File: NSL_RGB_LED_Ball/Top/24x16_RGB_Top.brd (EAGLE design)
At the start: 48 x 48 mm, 20 parts

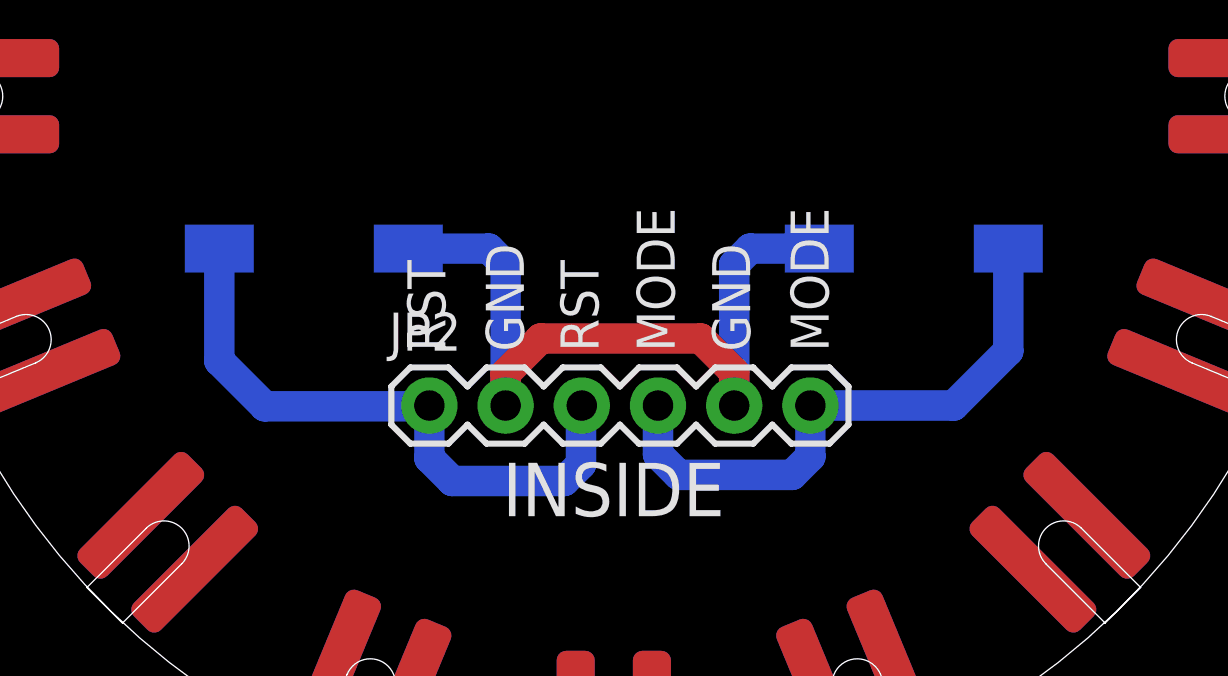
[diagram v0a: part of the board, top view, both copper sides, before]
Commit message: 
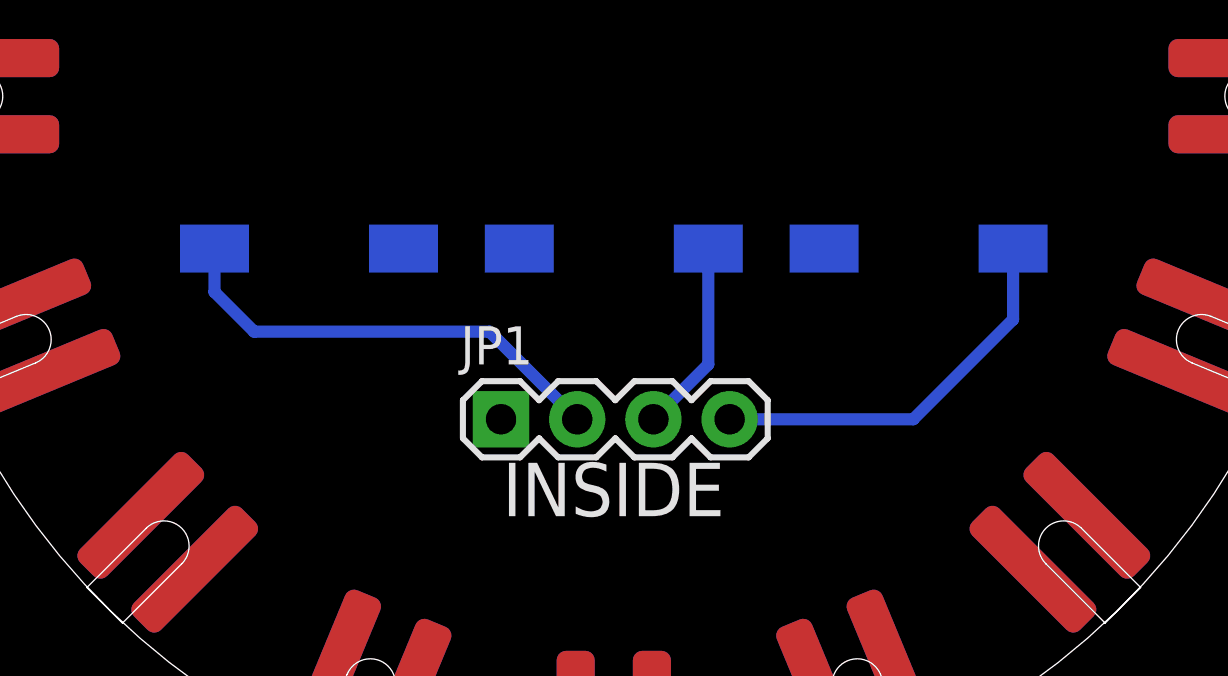
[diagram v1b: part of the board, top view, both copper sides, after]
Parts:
- removed JP2: (no value), SparkFun-Connectors:1X06
- added JP1: (no value), SparkFun-Connectors:1X04
- added S3: SPARKFUN-ELECTROMECHANICAL_SWITCH-MOMENTARY-2-SMD-1101NE, tvbgone-2layer:SPARKFUN-ELECTROMECHANICAL_TACTILE-SWITCH-1101NE
- moved S1 10.0 mm to (0.00, -5.08)
- moved S2 0.16 mm to (-10.2, -5.08)
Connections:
- removed net MODE: JP2.4, JP2.6, S1.P$1
- removed net RST: JP2.1, JP2.3, S2.P$1
- new net DOWN: JP1.2, S2.P$1
- new net SELECT: JP1.3, S1.P$1
- new net UP: JP1.4, S3.P$1
- net GND: now also JP1.1, S3.P$2; no longer JP2.2, JP2.5
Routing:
- net GND: track 26.7 -> 0.00 mm
- net RST: track 20.7 -> 0.00 mm
- net MODE: track 19.7 -> 0.00 mm
- net DOWN: track 0.00 -> 15.3 mm
- net UP: track 0.00 -> 13.2 mm
- net SELECT: track 0.00 -> 6.45 mm
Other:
- board text added: "DOWN"
- board text added: "SELECT"
- board text added: "UP"
- board text removed: "GND"
- board text removed: "MODE"
- board text removed: "Mode"
- board text removed: "RST"
- board text removed: "Reset"
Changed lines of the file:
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@@
 <wire x1="24" y1="0" x2="24" y2="0.01" width="0" layer="20" curve="-359.976127"/>
 <dimension x1="0" y1="-24" x2="0" y2="-21.16" x3="12.97" y3="-22.58" textsize="1.778" layer="48"/>
-<text x="-7.0612" y="-8.89" size="1.778" layer="22" font="vector" rot="MR0">Reset</text>
-<text x="13.081" y="-8.89" size="1.778" layer="22" font="vector" rot="MR0">Mode</text>
-<text x="-5.6134" y="-8.509" size="1.27" layer="21" font="vector" rot="R90">RST</text>
-<text x="-2.9972" y="-8.509" size="1.27" layer="21" font="vector" rot="R90">GND</text>
-<text x="2.032" y="-8.509" size="1.27" layer="21" font="vector" rot="R90">MODE</text>
-<text x="4.5466" y="-8.509" size="1.27" layer="21" font="vector" rot="R90">GND</text>
-<text x="7.1628" y="-8.509" size="1.27" layer="21" font="vector" rot="R90">MODE</text>
-<text x="-0.508" y="-8.509" size="1.27" layer="21" font="vector" rot="R90">RST</text>
 <text x="0" y="0" size="2.032" layer="22" font="vector" rot="MR0" align="center">nullspacelabs.com</text>
+<text x="11.3792" y="-9.144" size="1.778" layer="22" font="vector" rot="MR0">UP</text>
+<text x="4.6736" y="-9.144" size="1.778" layer="22" font="vector" rot="MR0">SELECT</text>
+<text x="-7.1628" y="-9.144" size="1.778" layer="22" font="vector" rot="MR0">DOWN</text>
 </plain>
 <attributes>
@@
 <attribute name="MF" value="" x="56.63675625" y="-45.45391875" size="1.778" layer="27" rot="R157.5" display="off"/>
 </element>
-<element name="S1" library="tvbgone-2layer" package="SPARKFUN-ELECTROMECHANICAL_TACTILE-SWITCH-1101NE" value="SPARKFUN-ELECTROMECHANICAL_SWITCH-MOMENTARY-2-SMD-1101NE" x="10" y="-5.08" rot="MR0"/>
-<element name="S2" library="tvbgone-2layer" package="SPARKFUN-ELECTROMECHANICAL_TACTILE-SWITCH-1101NE" value="SPARKFUN-ELECTROMECHANICAL_SWITCH-MOMENTARY-2-SMD-1101NE" x="-10" y="-5.08" rot="MR180"/>
-<element name="JP2" library="SparkFun-Connectors" package="1X06" value="" x="-6.1468" y="-10.3124"/>
+<element name="S1" library="tvbgone-2layer" package="SPARKFUN-ELECTROMECHANICAL_TACTILE-SWITCH-1101NE" value="SPARKFUN-ELECTROMECHANICAL_SWITCH-MOMENTARY-2-SMD-1101NE" x="0" y="-5.08" rot="MR0"/>
+<element name="S2" library="tvbgone-2layer" package="SPARKFUN-ELECTROMECHANICAL_TACTILE-SWITCH-1101NE" value="SPARKFUN-ELECTROMECHANICAL_SWITCH-MOMENTARY-2-SMD-1101NE" x="-10.16" y="-5.08" rot="MR180"/>
 <element name="U$1" library="24x16_RGB_Bottom" package="USB_PANNEL" value="USB_PANNEL" x="0" y="9.525"/>
+<element name="JP1" library="SparkFun-Connectors" package="1X04" value="" x="-3.7592" y="-10.7696"/>
+<element name="S3" library="tvbgone-2layer" package="SPARKFUN-ELECTROMECHANICAL_TACTILE-SWITCH-1101NE" value="SPARKFUN-ELECTROMECHANICAL_SWITCH-MOMENTARY-2-SMD-1101NE" x="10.16" y="-5.08" rot="MR0"/>
 </elements>
 <signals>
 <signal name="SLOT">
 </signal>
-<signal name="MODE">
-<contactref element="S1" pad="P$1"/>
-<contactref element="JP2" pad="6"/>
-<contactref element="JP2" pad="4"/>
-<wire x1="13.15" y1="-5.08" x2="13.15" y2="-8.4908" width="1.016" layer="16"/>
-<wire x1="13.15" y1="-8.4908" x2="11.3284" y2="-10.3124" width="1.016" layer="16"/>
-<wire x1="11.3284" y1="-10.3124" x2="6.5532" y2="-10.3124" width="1.016" layer="16"/>
-<wire x1="6.5532" y1="-10.3124" x2="6.5532" y2="-12.0142" width="1.016" layer="16"/>
-<wire x1="6.5532" y1="-12.0142" x2="5.9436" y2="-12.6238" width="1.016" layer="16"/>
-<wire x1="5.9436" y1="-12.6238" x2="2.159" y2="-12.6238" width="1.016" layer="16"/>
-<wire x1="2.159" y1="-12.6238" x2="1.4732" y2="-11.938" width="1.016" layer="16"/>
-<wire x1="1.4732" y1="-11.938" x2="1.4732" y2="-10.3124" width="1.016" layer="16"/>
-</signal>
-<signal name="RST">
-<contactref element="S2" pad="P$1"/>
-<contactref element="JP2" pad="1"/>
-<contactref element="JP2" pad="3"/>
-<wire x1="-13.15" y1="-5.08" x2="-13.15" y2="-8.821" width="1.016" layer="16"/>
-<wire x1="-13.15" y1="-8.821" x2="-11.6332" y2="-10.3378" width="1.016" layer="16"/>
-<wire x1="-11.6332" y1="-10.3378" x2="-6.1722" y2="-10.3378" width="1.016" layer="16"/>
-<wire x1="-6.1722" y1="-10.3378" x2="-6.1468" y2="-10.3124" width="1.016" layer="16"/>
-<wire x1="-6.1468" y1="-10.3124" x2="-6.1468" y2="-12.065" width="1.016" layer="16"/>
-<wire x1="-6.1468" y1="-12.065" x2="-5.3848" y2="-12.827" width="1.016" layer="16"/>
-<wire x1="-5.3848" y1="-12.827" x2="-1.651" y2="-12.827" width="1.016" layer="16"/>
-<wire x1="-1.651" y1="-12.827" x2="-1.0922" y2="-12.2682" width="1.016" layer="16"/>
-<wire x1="-1.0922" y1="-12.2682" x2="-1.0922" y2="-10.3378" width="1.016" layer="16"/>
-<wire x1="-1.0922" y1="-10.3378" x2="-1.0668" y2="-10.3124" width="1.016" layer="16"/>
-</signal>
 <signal name="GND">
 <contactref element="S1" pad="P$2"/>
 <contactref element="S2" pad="P$2"/>
-<contactref element="JP2" pad="5"/>
-<contactref element="JP2" pad="2"/>
-<wire x1="6.85" y1="-5.08" x2="4.5466" y2="-5.08" width="1.016" layer="16"/>
-<wire x1="4.5466" y1="-5.08" x2="4.0132" y2="-5.6134" width="1.016" layer="16"/>
-<wire x1="4.0132" y1="-5.6134" x2="4.0132" y2="-10.3124" width="1.016" layer="16"/>
-<wire x1="-6.85" y1="-5.08" x2="-4.1656" y2="-5.08" width="1.016" layer="16"/>
-<wire x1="-4.1656" y1="-5.08" x2="-3.6068" y2="-5.6388" width="1.016" layer="16"/>
-<wire x1="-3.6068" y1="-5.6388" x2="-3.6068" y2="-10.3124" width="1.016" layer="16"/>
-<wire x1="-3.6068" y1="-10.3124" x2="-3.6068" y2="-9.2456" width="1.016" layer="1"/>
-<wire x1="-3.6068" y1="-9.2456" x2="-2.4384" y2="-8.0772" width="1.016" layer="1"/>
-<wire x1="-2.4384" y1="-8.0772" x2="2.8956" y2="-8.0772" width="1.016" layer="1"/>
-<wire x1="2.8956" y1="-8.0772" x2="4.0132" y2="-9.1948" width="1.016" layer="1"/>
-<wire x1="4.0132" y1="-9.1948" x2="4.0132" y2="-10.3124" width="1.016" layer="1"/>
 <contactref element="SLOT1" pad="P$3"/>
 <contactref element="SLOT1" pad="P$4"/>
@@
 <vertex x="25.811" y="27.0204"/>
 </polygon>
+<contactref element="JP1" pad="1"/>
+<contactref element="S3" pad="P$2"/>
 </signal>
 <signal name="BLANK">
@@
 </polygon>
 </signal>
+<signal name="UP">
+<contactref element="JP1" pad="4"/>
+<contactref element="S3" pad="P$1"/>
+<wire x1="3.8608" y1="-10.7696" x2="9.9822" y2="-10.7696" width="0.4064" layer="16"/>
+<wire x1="9.9822" y1="-10.7696" x2="13.3096" y2="-7.4422" width="0.4064" layer="16"/>
+<wire x1="13.3096" y1="-7.4422" x2="13.3096" y2="-5.0804" width="0.4064" layer="16"/>
+<wire x1="13.3096" y1="-5.0804" x2="13.31" y2="-5.08" width="0.4064" layer="16"/>
+</signal>
+<signal name="SELECT">
+<contactref element="JP1" pad="3"/>
+<contactref element="S1" pad="P$1"/>
+<wire x1="1.3208" y1="-10.7696" x2="3.15" y2="-8.9404" width="0.4064" layer="16"/>
+<wire x1="3.15" y1="-8.9404" x2="3.15" y2="-5.08" width="0.4064" layer="16"/>
+</signal>
+<signal name="DOWN">
+<contactref element="JP1" pad="2"/>
+<contactref element="S2" pad="P$1"/>
+<wire x1="-1.2192" y1="-10.7696" x2="-4.1402" y2="-7.8486" width="0.4064" layer="16"/>
+<wire x1="-4.1402" y1="-7.8486" x2="-11.9888" y2="-7.8486" width="0.4064" layer="16"/>
+<wire x1="-11.9888" y1="-7.8486" x2="-13.31" y2="-6.5274" width="0.4064" layer="16"/>
+<wire x1="-13.31" y1="-6.5274" x2="-13.31" y2="-5.08" width="0.4064" layer="16"/>
+</signal>
 </signals>

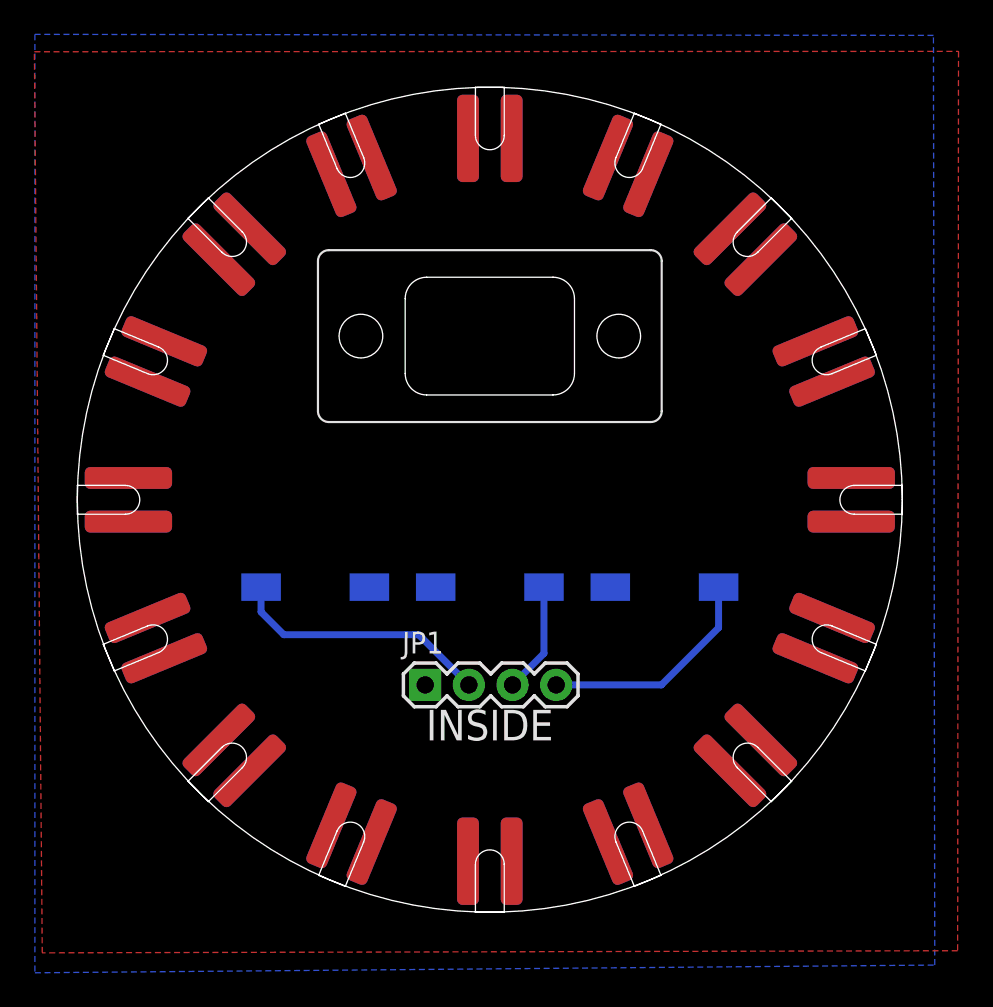
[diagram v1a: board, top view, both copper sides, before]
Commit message: 
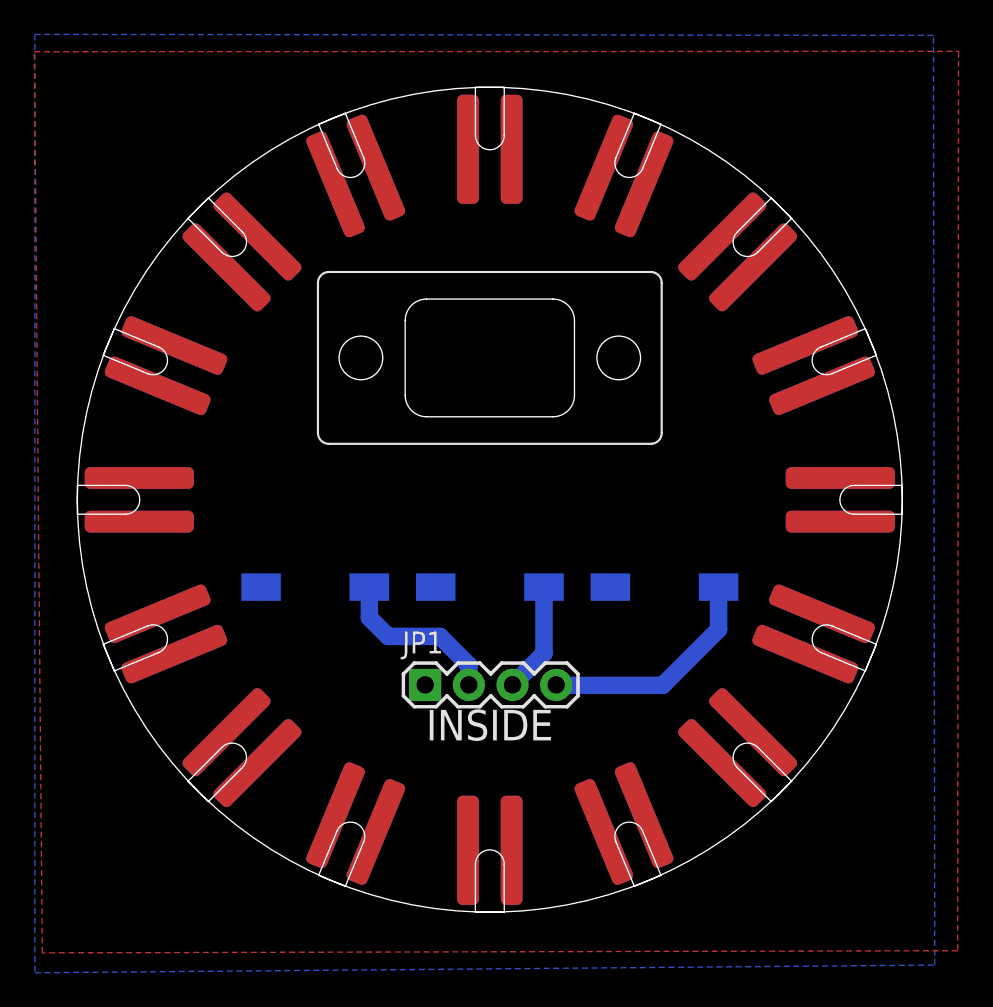
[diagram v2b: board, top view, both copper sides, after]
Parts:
- SLOT1, SLOT10, SLOT11, SLOT12, SLOT13, SLOT14, SLOT15, SLOT16, SLOT2, SLOT3, SLOT4, SLOT5, SLOT6, SLOT7, SLOT8, SLOT9: device 24x16_RGB_Bottom:SLOT -> 24x16_RGB_Top:SLOT
- moved U$1 1.27 mm to (0.00, 8.26)
- turned S2 to 0 degrees
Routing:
- net DOWN: track 15.3 -> 9.86 mm

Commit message: 
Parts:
- removed JP1: (no value), SparkFun-Connectors:1X04
- added JP2: (no value), SparkFun-Connectors:1X06
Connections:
- net DOWN: now also JP2.4; no longer JP1.2
- net GND: now also JP2.1, JP2.2, JP2.3; no longer JP1.1
- net SELECT: now also JP2.5; no longer JP1.3
- net UP: now also JP2.6; no longer JP1.4
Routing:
- net UP: track 13.3 -> 9.32 mm
- net DOWN: track 9.86 -> 10.8 mm
- net SELECT: track 6.45 -> 5.90 mm
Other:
- board text added: "DWN"
- board text added: "GND"
- board text added: "SEL"
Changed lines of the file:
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@@
 <plain>
 <text x="0" y="-15.2108" size="1.778" layer="22" rot="MR0" align="center">A</text>
-<text x="-3.71" y="-14" size="1.778" layer="21">INSIDE</text>
+<text x="-3.6592" y="-3.1796" size="1.778" layer="21">INSIDE</text>
 <wire x1="24" y1="0" x2="24" y2="0.01" width="0" layer="20" curve="-359.976127"/>
 <dimension x1="0" y1="-24" x2="0" y2="-21.16" x3="12.97" y3="-22.58" textsize="1.778" layer="48"/>
@@
 <text x="4.6736" y="-9.144" size="1.778" layer="22" font="vector" rot="MR0">SELECT</text>
 <text x="-7.1628" y="-9.144" size="1.778" layer="22" font="vector" rot="MR0">DOWN</text>
+<text x="0.381" y="-12.065" size="1.778" layer="21" font="vector" rot="R270">DWN</text>
+<text x="2.9718" y="-12.065" size="1.778" layer="21" font="vector" rot="R270">SEL</text>
+<text x="5.6388" y="-12.065" size="1.778" layer="21" font="vector" rot="R270">UP</text>
+<text x="-2.1336" y="-12.065" size="1.778" layer="21" font="vector" rot="R270">GND</text>
+<text x="-4.6482" y="-12.065" size="1.778" layer="21" font="vector" rot="R270">GND</text>
+<text x="-7.2644" y="-12.065" size="1.778" layer="21" font="vector" rot="R270">GND</text>
 </plain>
 <attributes>
@@
 </element>
 <element name="U$1" library="24x16_RGB_Bottom" package="USB_PANNEL" value="USB_PANNEL" x="0" y="8.255"/>
-<element name="JP1" library="SparkFun-Connectors" package="1X04" value="" x="-3.7592" y="-10.7696"/>
 <element name="S3" library="tvbgone-2layer" package="SPARKFUN-ELECTROMECHANICAL_TACTILE-SWITCH-1101NE" value="SPARKFUN-ELECTROMECHANICAL_SWITCH-MOMENTARY-2-SMD-1101NE" x="10.16" y="-5.08" smashed="yes" rot="MR0">
 <attribute name="NAME" x="13.16" y="-3.08" size="0.762" layer="26" rot="MR0"/>
 </element>
+<element name="JP2" library="SparkFun-Connectors" package="1X06" value="" x="-6.3754" y="-10.7188"/>
 </elements>
 <signals>
@@
 <vertex x="25.811" y="27.0204"/>
 </polygon>
-<contactref element="JP1" pad="1"/>
 <contactref element="S3" pad="P$2"/>
+<contactref element="JP2" pad="3"/>
+<contactref element="JP2" pad="2"/>
+<contactref element="JP2" pad="1"/>
 </signal>
 <signal name="BLANK">
@@
 </signal>
 <signal name="UP">
-<contactref element="JP1" pad="4"/>
 <contactref element="S3" pad="P$1"/>
 <wire x1="13.3096" y1="-5.0804" x2="13.31" y2="-5.08" width="0.4064" layer="16"/>
-<wire x1="3.8608" y1="-10.7696" x2="3.8862" y2="-10.795" width="1.016" layer="16"/>
-<wire x1="3.8862" y1="-10.795" x2="10.0584" y2="-10.795" width="1.016" layer="16"/>
-<wire x1="10.0584" y1="-10.795" x2="13.31" y2="-7.5434" width="1.016" layer="16"/>
-<wire x1="13.31" y1="-7.5434" x2="13.31" y2="-5.08" width="1.016" layer="16"/>
+<contactref element="JP2" pad="6"/>
+<wire x1="13.31" y1="-5.08" x2="7.6712" y2="-10.7188" width="0.4064" layer="16"/>
+<wire x1="7.6712" y1="-10.7188" x2="6.3246" y2="-10.7188" width="0.4064" layer="16"/>
 </signal>
 <signal name="SELECT">
-<contactref element="JP1" pad="3"/>
 <contactref element="S1" pad="P$1"/>
-<wire x1="1.3208" y1="-10.7696" x2="3.15" y2="-8.9404" width="1.016" layer="16"/>
-<wire x1="3.15" y1="-8.9404" x2="3.15" y2="-5.08" width="1.016" layer="16"/>
+<contactref element="JP2" pad="5"/>
+<wire x1="3.15" y1="-5.08" x2="3.7846" y2="-5.7146" width="0.4064" layer="16"/>
+<wire x1="3.7846" y1="-5.7146" x2="3.7846" y2="-10.7188" width="0.4064" layer="16"/>
 </signal>
 <signal name="DOWN">
-<contactref element="JP1" pad="2"/>
 <contactref element="S2" pad="P$1"/>
-<wire x1="-1.2192" y1="-10.7696" x2="-1.2192" y2="-9.6266" width="1.016" layer="16"/>
-<wire x1="-1.2192" y1="-9.6266" x2="-2.8956" y2="-7.9502" width="1.016" layer="16"/>
-<wire x1="-2.8956" y1="-7.9502" x2="-5.9182" y2="-7.9502" width="1.016" layer="16"/>
-<wire x1="-5.9182" y1="-7.9502" x2="-7.01" y2="-6.8584" width="1.016" layer="16"/>
-<wire x1="-7.01" y1="-6.8584" x2="-7.01" y2="-5.08" width="1.016" layer="16"/>
+<contactref element="JP2" pad="4"/>
+<wire x1="-7.01" y1="-5.08" x2="-3.9112" y2="-8.1788" width="0.4064" layer="16"/>
+<wire x1="-3.9112" y1="-8.1788" x2="-0.8636" y2="-8.1788" width="0.4064" layer="16"/>
+<wire x1="-0.8636" y1="-8.1788" x2="1.2446" y2="-10.287" width="0.4064" layer="16"/>
+<wire x1="1.2446" y1="-10.287" x2="1.2446" y2="-10.7188" width="0.4064" layer="16"/>
 </signal>
 </signals>

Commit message: 
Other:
- board text added: "M"
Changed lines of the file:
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@@
 <text x="-4.6482" y="-12.065" size="1.778" layer="21" font="vector" rot="R270">GND</text>
 <text x="-7.2644" y="-12.065" size="1.778" layer="21" font="vector" rot="R270">GND</text>
+<text x="10.8458" y="-10.5918" size="2.54" layer="16" font="vector" rot="MR0" align="center">M</text>
 </plain>
 <attributes>
